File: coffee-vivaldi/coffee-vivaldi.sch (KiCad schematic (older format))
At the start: 87 parts, among them J2 AudioPlug3, SW1 SW_SPDT, U1 Opamp_Quad_Generic, U3 OPA1604

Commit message: Deleted two SMA connectors
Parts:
- removed U? (x2): SMA_PCB_Edge_Mount, symbol HS2_Parts:SMA_PCB_Edge_Mount
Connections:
- net COUPLER_SIGNAL: now also R?.1
- net RF_OUT1: now reaches U?.2 (SIGNAL)
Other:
- moved on the sheet: R?, U?
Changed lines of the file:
@@
-$Comp
-L HS2_Parts:SMA_PCB_Edge_Mount U?
-U 1 1 60438739
-P 13700 1500
-F 0 "U?" H 13600 1300 50  0000 C CNN
-F 1 "SMA_PCB_Edge_Mount" H 13550 1400 50  0000 C CNN
-F 2 "" H 13700 1500 50  0001 C CNN
-F 3 "" H 13700 1500 50  0001 C CNN
-	1    13700 1500
-	1    0    0    -1
-$EndComp
 $Comp
 L HS2_Parts:SMA_PCB_Edge_Mount U?
 U 1 1 6043955D
-P 15550 1100
-F 0 "U?" H 15450 900 50  0000 C CNN
-F 1 "SMA_PCB_Edge_Mount" H 15400 1000 50  0000 C CNN
-F 2 "" H 15550 1100 50  0001 C CNN
-F 3 "" H 15550 1100 50  0001 C CNN
-	1    15550 1100
+P 14800 1250
+F 0 "U?" H 14700 1050 50  0000 C CNN
+F 1 "SMA_PCB_Edge_Mount" H 14650 1150 50  0000 C CNN
+F 2 "" H 14800 1250 50  0001 C CNN
+F 3 "" H 14800 1250 50  0001 C CNN
+	1    14800 1250
 	-1   0    0    1
 $EndComp
 Wire Wire Line
 	12150 2850 13050 2850
-Wire Wire Line
-	13200 3400 13450 3400
-Wire Wire Line
-	13450 3400 13450 3250
-Wire Wire Line
-	13450 3250 13750 3250
-Wire Wire Line
-	14000 1300 15250 1300
 $Comp
-L HS2_Parts:SMA_PCB_Edge_Mount U?
-U 1 1 604AA8E4
-P 13700 2100
-F 0 "U?" H 13600 1900 50  0000 C CNN
-F 1 "SMA_PCB_Edge_Mount" H 13550 2000 50  0000 C CNN
-F 2 "" H 13700 2100 50  0001 C CNN
-F 3 "" H 13700 2100 50  0001 C CNN
-	1    13700 2100
+L power:GND #PWR?
+U 1 1 604BDAC7
+P 14650 2600
+F 0 "#PWR?" H 14650 2350 50  0001 C CNN
+F 1 "GND" H 14655 2427 50  0000 C CNN
+F 2 "" H 14650 2600 50  0001 C CNN
+F 3 "" H 14650 2600 50  0001 C CNN
+	1    14650 2600
 	1    0    0    -1
 $EndComp
 $Comp
 L power:GND #PWR?
-U 1 1 604BD349
-P 14250 1700
-F 0 "#PWR?" H 14250 1450 50  0001 C CNN
-F 1 "GND" H 14255 1527 50  0000 C CNN
-F 2 "" H 14250 1700 50  0001 C CNN
-F 3 "" H 14250 1700 50  0001 C CNN
-	1    14250 1700
-	1    0    0    -1
-$EndComp
-$Comp
-L power:GND #PWR?
-U 1 1 604BD6D7
-P 14250 2050
-F 0 "#PWR?" H 14250 1800 50  0001 C CNN
-F 1 "GND" H 14255 1877 50  0000 C CNN
-F 2 "" H 14250 2050 50  0001 C CNN
-F 3 "" H 14250 2050 50  0001 C CNN
-	1    14250 2050
-	1    0    0    -1
-$EndComp
-$Comp
-L power:GND #PWR?
-U 1 1 604BDAC7
-P 15400 2450
-F 0 "#PWR?" H 15400 2200 50  0001 C CNN
-F 1 "GND" H 15405 2277 50  0000 C CNN
-F 2 "" H 15400 2450 50  0001 C CNN
-F 3 "" H 15400 2450 50  0001 C CNN
-	1    15400 2450
+U 1 1 60527B36
+P 14150 1200
+F 0 "#PWR?" H 14150 950 50  0001 C CNN
+F 1 "GND" H 14155 1027 50  0000 C CNN
+F 2 "" H 14150 1200 50  0001 C CNN
+F 3 "" H 14150 1200 50  0001 C CNN
+	1    14150 1200
 	1    0    0    -1
 $EndComp
 Wire Wire Line
-	14250 1700 14000 1700
+	14150 1200 14500 1200
 Wire Wire Line
-	14000 1700 14000 1800
-Wire Wire Line
-	14000 2000 14250 2000
-Wire Wire Line
-	14250 2000 14250 2050
+	14500 1200 14500 1350
 $Comp
 L power:GND #PWR?
-U 1 1 605037D3
-P 14150 1450
-F 0 "#PWR?" H 14150 1200 50  0001 C CNN
-F 1 "GND" H 14155 1277 50  0000 C CNN
-F 2 "" H 14150 1450 50  0001 C CNN
-F 3 "" H 14150 1450 50  0001 C CNN
-	1    14150 1450
+U 1 1 6053A413
+P 14300 1650
+F 0 "#PWR?" H 14300 1400 50  0001 C CNN
+F 1 "GND" H 14305 1477 50  0000 C CNN
+F 2 "" H 14300 1650 50  0001 C CNN
+F 3 "" H 14300 1650 50  0001 C CNN
+	1    14300 1650
 	1    0    0    -1
 $EndComp
 Wire Wire Line
-	14000 1400 14150 1400
+	14300 1650 14300 1550
 Wire Wire Line
-	14150 1400 14150 1450
+	14300 1550 14500 1550
 $Comp
-L power:GND #PWR?
-U 1 1 6051563D
-P 14200 1050
-F 0 "#PWR?" H 14200 800 50  0001 C CNN
-F 1 "GND" H 14205 877 50  0000 C CNN
-F 2 "" H 14200 1050 50  0001 C CNN
-F 3 "" H 14200 1050 50  0001 C CNN
-	1    14200 1050
+L Device:R R?
+U 1 1 6058F77C
+P 14650 2300
+F 0 "R?" H 14720 2346 50  0000 L CNN
+F 1 "50" H 14720 2255 50  0000 L CNN
+F 2 "" V 14580 2300 50  0001 C CNN
+F 3 "~" H 14650 2300 50  0001 C CNN
+	1    14650 2300
 	1    0    0    -1
 $EndComp
 Wire Wire Line
-	14000 1200 14100 1200
+	14650 2450 14650 2600
 Wire Wire Line
-	14100 1200 14100 1050
+	14650 2050 14650 2150
 Wire Wire Line
-	14100 1050 14200 1050
-$Comp
-L power:GND #PWR?
-U 1 1 60527B36
-P 14900 1050
-F 0 "#PWR?" H 14900 800 50  0001 C CNN
-F 1 "GND" H 14905 877 50  0000 C CNN
-F 2 "" H 14900 1050 50  0001 C CNN
-F 3 "" H 14900 1050 50  0001 C CNN
-	1    14900 1050
-	1    0    0    -1
-$EndComp
+	13900 1450 14500 1450
+Text GLabel 13900 1450 0    50   Input ~ 0
+RF_OUT1
+Text GLabel 14250 2050 0    50   Input ~ 0
+COUPLER_SIGNAL
 Wire Wire Line
-	14900 1050 15250 1050
-Wire Wire Line
-	15250 1050 15250 1200
-$Comp
-L power:GND #PWR?
-U 1 1 6053A413
-P 15050 1500
-F 0 "#PWR?" H 15050 1250 50  0001 C CNN
-F 1 "GND" H 15055 1327 50  0000 C CNN
-F 2 "" H 15050 1500 50  0001 C CNN
-F 3 "" H 15050 1500 50  0001 C CNN
-	1    15050 1500
-	1    0    0    -1
-$EndComp
-Wire Wire Line
-	15050 1500 15050 1400
-Wire Wire Line
-	15050 1400 15250 1400
-$Comp
-L power:GND #PWR?
-U 1 1 6054DD37
-P 13750 3450
-F 0 "#PWR?" H 13750 3200 50  0001 C CNN
-F 1 "GND" H 13755 3277 50  0000 C CNN
-F 2 "" H 13750 3450 50  0001 C CNN
-F 3 "" H 13750 3450 50  0001 C CNN
-	1    13750 3450
-	1    0    0    -1
-$EndComp
-Wire Wire Line
-	13750 3250 13750 3450
-$Comp
-L Device:R R?
-U 1 1 6058F77C
-P 15400 2150
-F 0 "R?" H 15470 2196 50  0000 L CNN
-F 1 "50" H 15470 2105 50  0000 L CNN
-F 2 "" V 15330 2150 50  0001 C CNN
-F 3 "~" H 15400 2150 50  0001 C CNN
-	1    15400 2150
-	1    0    0    -1
-$EndComp
-Wire Wire Line
-	15400 2300 15400 2450
-Wire Wire Line
-	15400 1900 15400 2000
-Wire Wire Line
-	14000 1900 15400 1900
-Wire Wire Line
-	13750 3250 14050 3250
-Connection ~ 13750 3250
-Text Label 13200 3400 2    50   ~ 0
-RF_OUT1
-Text Label 14050 3250 0    50   ~ 0
-COUPLER_PORT1
+	14250 2050 14650 2050
 $EndSCHEMATC

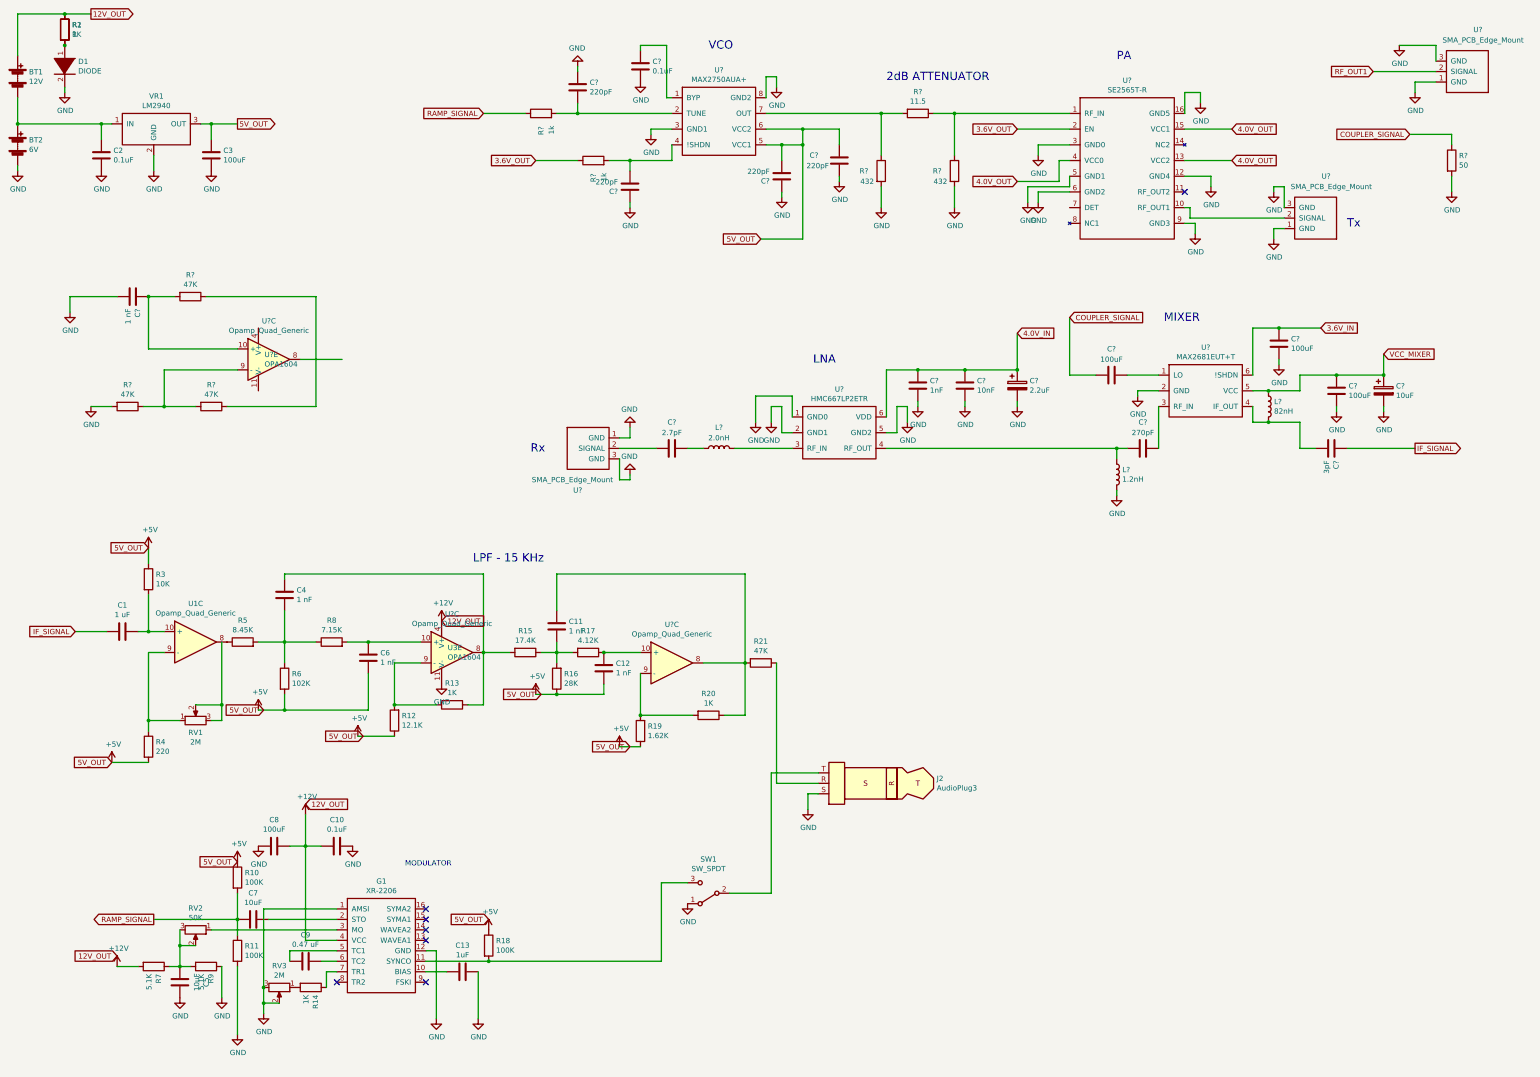
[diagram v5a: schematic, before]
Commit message: Added voltage dividers
Still need to work on mixer, LPF, and how to interface the audio jack from a pcb.
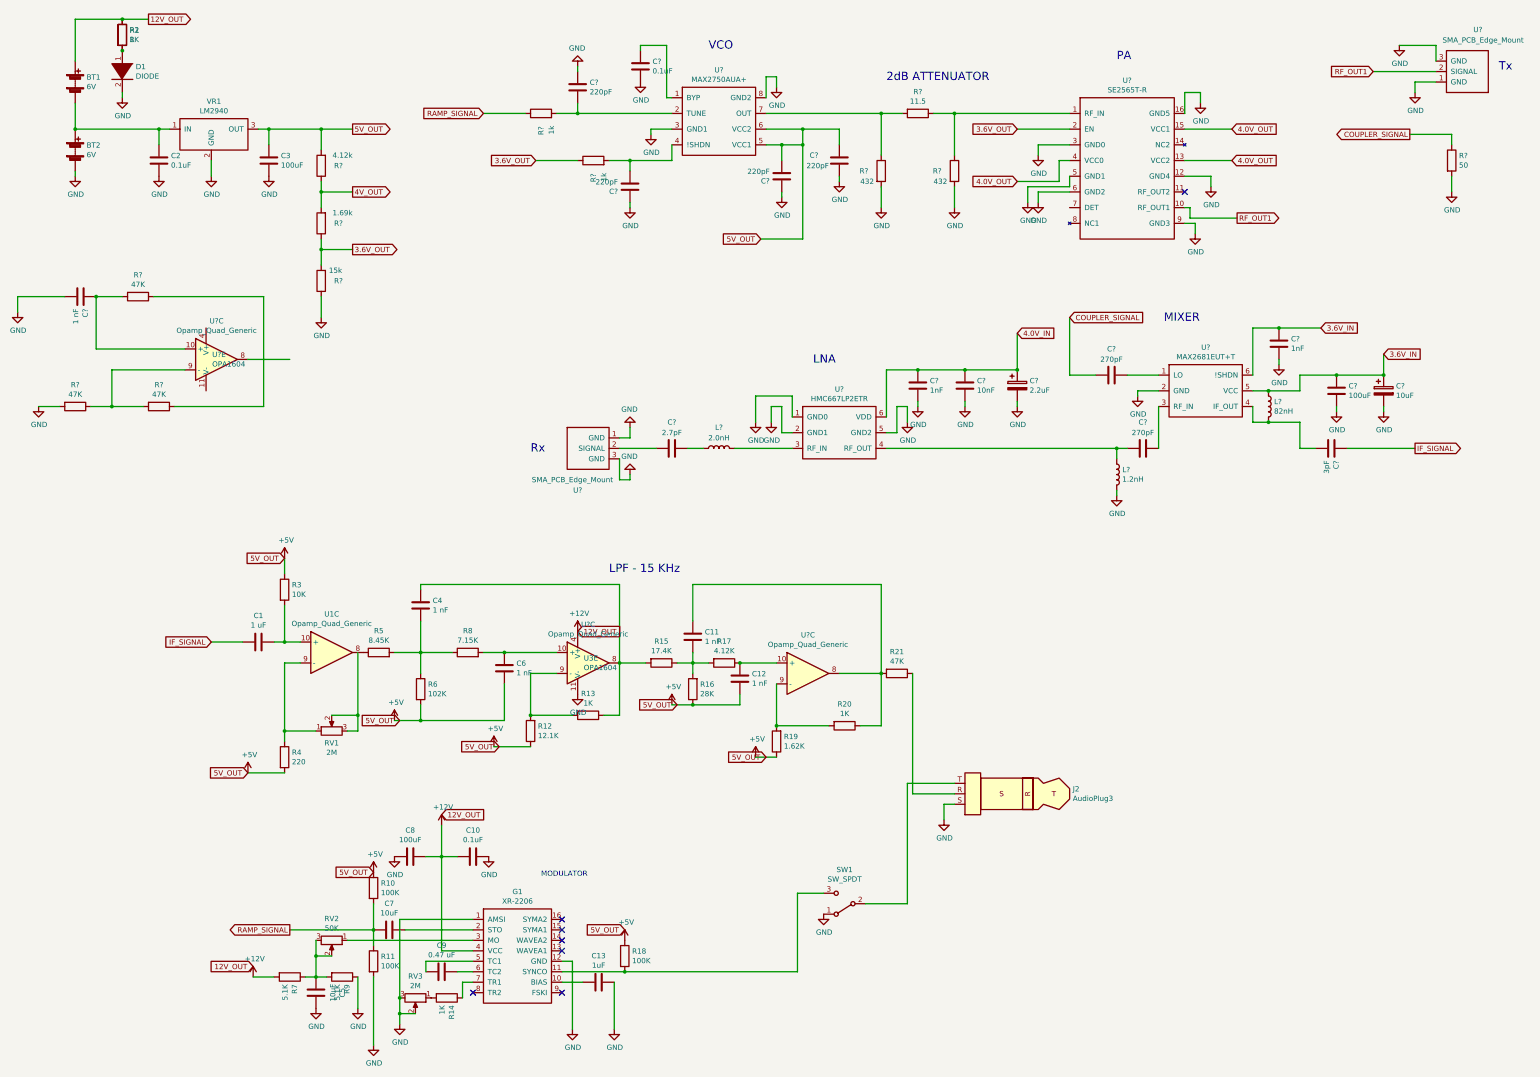
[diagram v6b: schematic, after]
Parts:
- removed U?: SMA_PCB_Edge_Mount, symbol HS2_Parts:SMA_PCB_Edge_Mount
- added R?: 4.12k, symbol Device:R
- added R?: 1.69k, symbol Device:R
- added R?: 15k, symbol Device:R
- BT1: value 12V -> 6V
- C?: value 100uF -> 270pF
- C?: value 100uF -> 1nF
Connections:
- net VCC_MIXER is gone; now on net 3.6V_IN: C?.1, C?.1, L?.1, U?.5 (VCC)
- net +5V: now also R?.2
- net 3.6V_OUT: now also R?.1, R?.2
- net GND: now also R?.1
- net RF_OUT1: now also U?.10 (RF_OUT1)
- new net 4V_OUT: R?.1, R?.2
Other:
- moved on the sheet: BT1, BT2, C1, C10, C11, C12, C13, C2, C3, C4, C5, C6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

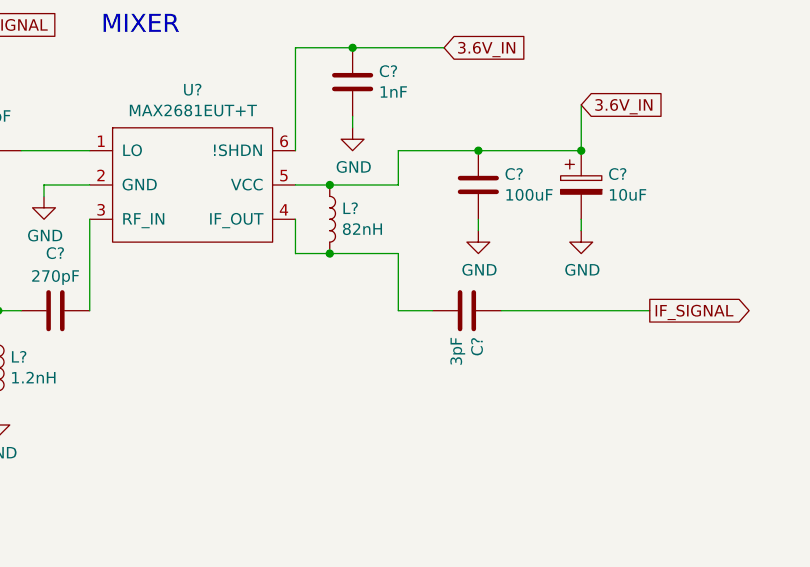
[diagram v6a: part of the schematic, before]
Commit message: Update coffee-vivaldi.sch
Current mixer RF input frequency is 2450 MHz, IF output frequency 45 MHz. Will need to double-check if this will affect how we process this signal.
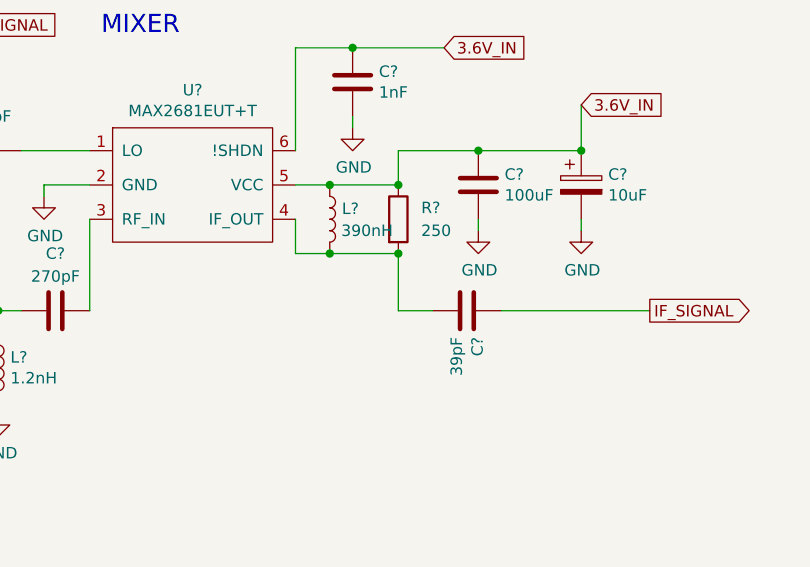
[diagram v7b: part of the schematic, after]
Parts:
- added R?: 250, symbol Device:R
- C?: value 3pF -> 39pF
- L?: value 82nH -> 390nH
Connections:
- net 3.6V_IN: now also R?.1
- net at C?.2, L?.2, U?.4 (IF_OUT): now also R?.2
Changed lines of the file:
@@
 P 12900 4650
 F 0 "L?" H 12953 4696 50  0000 L CNN
-F 1 "82nH" H 12953 4605 50  0000 L CNN
+F 1 "390nH" H 12950 4600 50  0000 L CNN
 F 2 "" H 12900 4650 50  0001 C CNN
 F 3 "~" H 12900 4650 50  0001 C CNN
@@
 P 13500 5050
 F 0 "C?" H 13615 5096 50  0000 L CNN
-F 1 "3pF" H 13615 5005 50  0000 L CNN
+F 1 "39pF" H 13615 5005 50  0000 L CNN
 F 2 "" H 13538 4900 50  0001 C CNN
 F 3 "~" H 13500 5050 50  0001 C CNN
@@
 Wire Wire Line
 	3850 2000 4150 2000
+$Comp
+L Device:R R?
+U 1 1 604250C0
+P 13200 4650
+F 0 "R?" H 13300 4700 50  0000 L CNN
+F 1 "250" H 13300 4600 50  0000 L CNN
+F 2 "" V 13130 4650 50  0001 C CNN
+F 3 "~" H 13200 4650 50  0001 C CNN
+	1    13200 4650
+	1    0    0    -1
+$EndComp
+Connection ~ 13200 4500
+Connection ~ 13200 4800
 $EndSCHEMATC
